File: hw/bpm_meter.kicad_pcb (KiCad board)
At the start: 2 copper layers, 60 x 50 mm, 85 parts, among them J1 Conn_01x06_Pin, J2 Conn_01x03_Pin, J901 USB_C_Receptacle_USB2.0, Q1 AO3400A, SW901 SW_MEC_5E, U1 AOZ1282CI, U10 IS31FL3236A, U11 SLS0391FR1A1GD, U12 SLS0391FR1A1GD, U13 SLS0391FR1A1GD, U2 AMS1117-3.3, U3 H11L1, U901 RP2040, U902 AMS1117-3.3, U903 W25Q128JVS, Y901 Crystal_GND24_Small

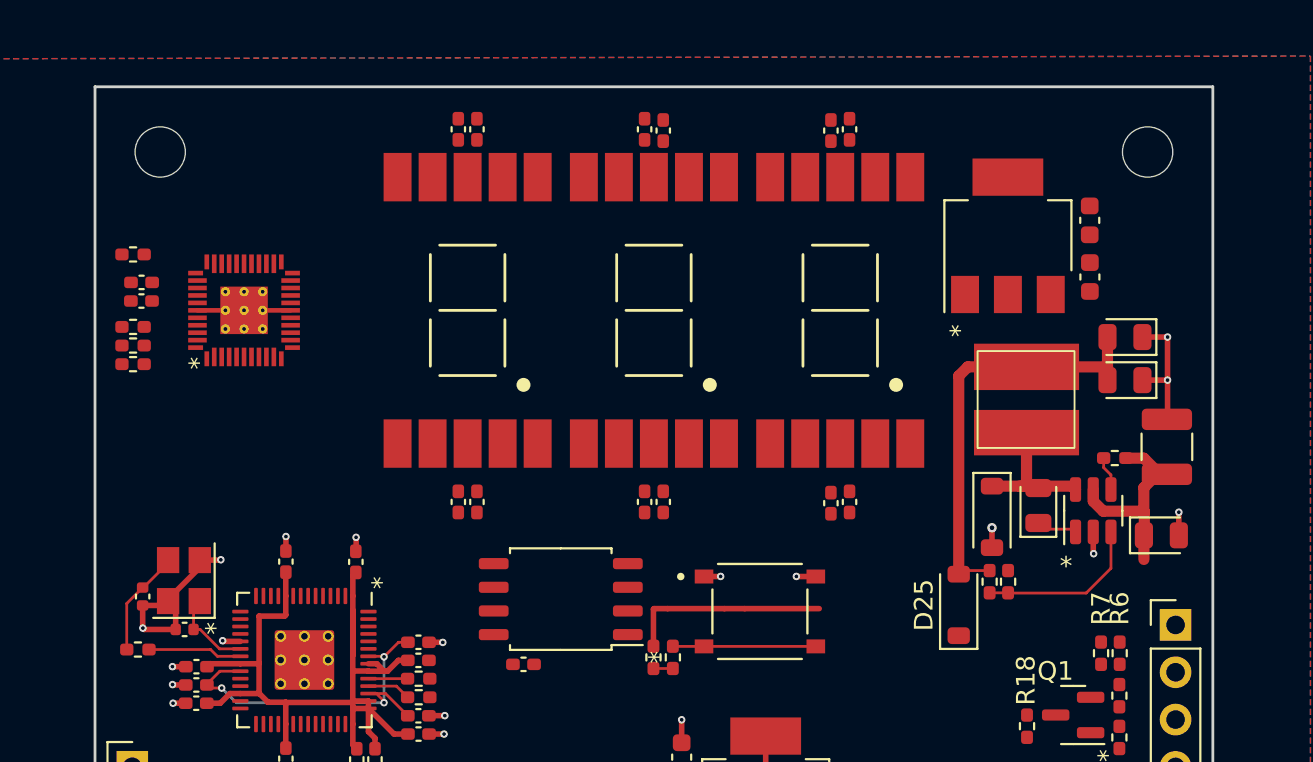
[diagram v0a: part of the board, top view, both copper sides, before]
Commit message: Routed part of the design
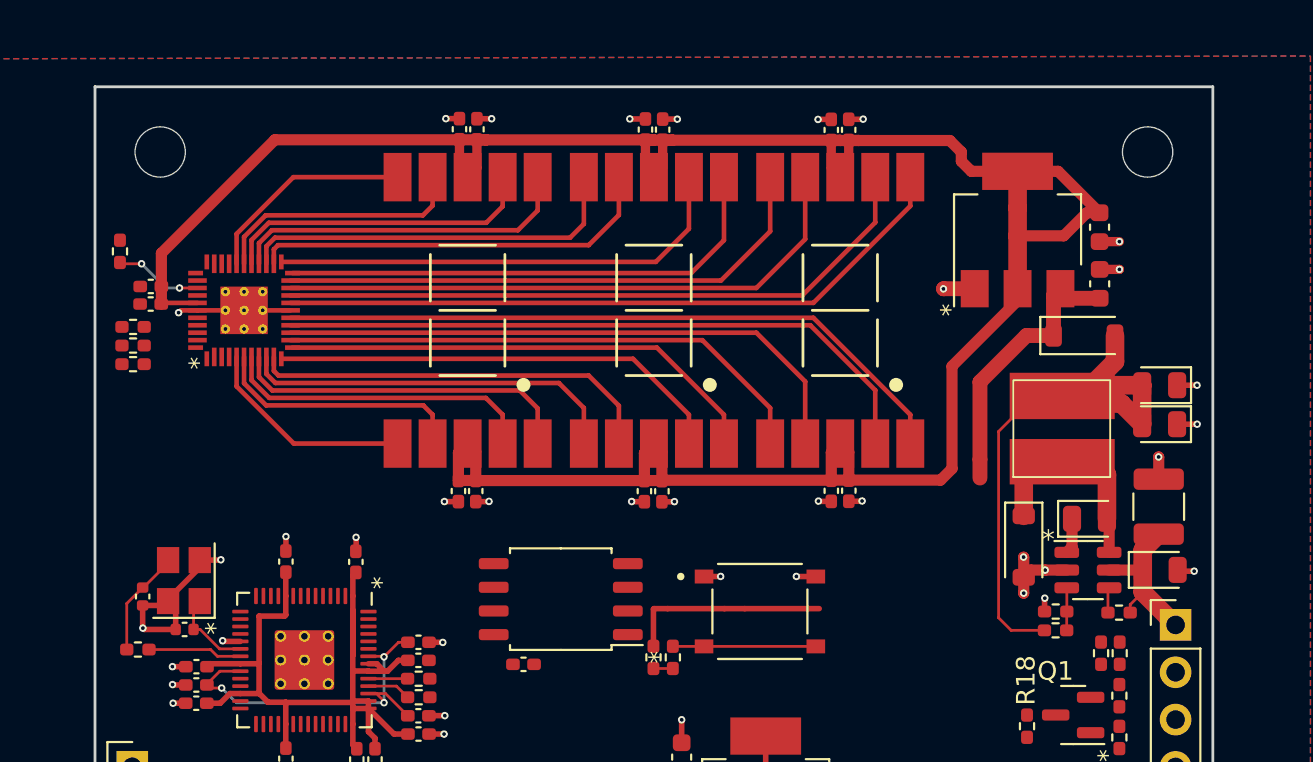
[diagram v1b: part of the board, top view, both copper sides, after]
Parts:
- moved D25 16.0 mm to (153.1, 113.4), turned to 0 degrees
- moved R11 8.30 mm to (155.0, 128.2)
- moved R12 4.40 mm to (151.6, 129.2), turned to 180 degrees
- moved C1 3.24 mm to (157.1, 122.5)
- moved U1 3.20 mm to (153.3, 125.9), turned to 0 degrees
- moved C5 3.19 mm to (157.1, 116.0)
- moved R13 3.02 mm to (151.6, 128.2), turned to 180 degrees
- moved C4 3.01 mm to (157.1, 118.1)
- moved C3 2.84 mm to (153.4, 123.2), turned to 0 degrees
- moved L1 2.47 mm to (152.0, 118.3)
- moved D24 2.33 mm to (149.8, 124.7)
- moved C2 1.86 mm to (157.2, 125.9)
- moved C24 1.26 mm to (103.0, 111.7)
- moved C16 1.17 mm to (140.5, 121.7), turned to -90 degrees
- moved C14 1.17 mm to (129.5, 121.7), turned to -90 degrees
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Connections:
- U10 pad 10: unconnected-(U10-OUT12-Pad10) -> Net-(U10-OUT12)
- U10 pad 11: unconnected-(U10-OUT13-Pad11) -> Net-(U10-OUT13)
- U10 pad 12: unconnected-(U10-OUT14-Pad12) -> Net-(U10-OUT14)
- U10 pad 2: Net-(U10-OUT4) -> unconnected-(U10-OUT4-Pad2)
- U10 pad 22: unconnected-(U10-OUT23-Pad22) -> Net-(U10-OUT23)
- U10 pad 23: unconnected-(U10-OUT24-Pad23) -> Net-(U10-OUT24)
- U10 pad 24: unconnected-(U10-OUT25-Pad24) -> Net-(U10-OUT25)
- U10 pad 3: Net-(U10-OUT5) -> unconnected-(U10-OUT5-Pad3)
- U10 pad 30: Net-(U10-OUT31) -> unconnected-(U10-OUT31-Pad30)
- U10 pad 31: Net-(U10-OUT32) -> unconnected-(U10-OUT32-Pad31)
- U10 pad 32: Net-(U10-OUT33) -> unconnected-(U10-OUT33-Pad32)
- U10 pad 4: Net-(U10-OUT6) -> unconnected-(U10-OUT6-Pad4)
- U11 pad 1: Net-(U10-OUT8) -> Net-(U10-OUT7)
- U11 pad 10: Net-(U10-OUT10) -> Net-(U10-OUT30)
- U11 pad 2: Net-(U10-OUT7) -> Net-(U10-OUT8)
- U11 pad 4: Net-(U10-OUT6) -> Net-(U10-OUT9)
- U11 pad 5: Net-(U10-OUT11) -> Net-(U10-OUT10)
- U11 pad 6: Net-(U10-OUT5) -> Net-(U10-OUT27)
- U11 pad 7: Net-(U10-OUT4) -> Net-(U10-OUT28)
- U11 pad 9: Net-(U10-OUT9) -> Net-(U10-OUT29)
- U12 pad 1: Net-(U10-OUT19) -> Net-(U10-OUT11)
- U12 pad 10: Net-(U10-OUT21) -> Net-(U10-OUT26)
- U12 pad 2: Net-(U10-OUT18) -> Net-(U10-OUT12)
- U12 pad 4: Net-(U10-OUT17) -> Net-(U10-OUT13)
- U12 pad 5: Net-(U10-OUT22) -> Net-(U10-OUT14)
- U12 pad 6: Net-(U10-OUT16) -> Net-(U10-OUT23)
- U12 pad 7: Net-(U10-OUT15) -> Net-(U10-OUT24)
- U12 pad 9: Net-(U10-OUT20) -> Net-(U10-OUT25)
- U13 pad 1: Net-(U10-OUT30) -> Net-(U10-OUT15)
- U13 pad 10: Net-(U10-OUT32) -> Net-(U10-OUT22)
- U13 pad 2: Net-(U10-OUT29) -> Net-(U10-OUT16)
- U13 pad 4: Net-(U10-OUT28) -> Net-(U10-OUT17)
- U13 pad 5: Net-(U10-OUT33) -> Net-(U10-OUT18)
- U13 pad 6: Net-(U10-OUT27) -> Net-(U10-OUT19)
- U13 pad 7: Net-(U10-OUT26) -> Net-(U10-OUT20)
- U13 pad 9: Net-(U10-OUT31) -> Net-(U10-OUT21)
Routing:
- net +3.3VP: track 0.00 -> 137.3 mm
- net Net-(U10-OUT19): track 0.00 -> 37.0 mm
- net Net-(U10-OUT18): track 0.00 -> 37.0 mm
- net Net-(U10-OUT17): track 0.00 -> 35.7 mm
- net Net-(U10-OUT20): track 0.00 -> 35.4 mm
- net Net-(U10-OUT21): track 0.00 -> 32.0 mm
- net Net-(U10-OUT16): track 0.00 -> 32.0 mm
- net Net-(U10-OUT22): track 0.00 -> 29.7 mm
- net Net-(U10-OUT15): track 0.00 -> 29.2 mm
- net Net-(U10-OUT23): track 0.00 -> 27.3 mm
- net Net-(U10-OUT14): track 0.00 -> 26.2 mm
- net Net-(U10-OUT24): track 0.00 -> 25.4 mm
- net Net-(U10-OUT13): track 0.00 -> 24.7 mm
- net Net-(U10-OUT25): track 0.00 -> 22.1 mm
- net Net-(U10-OUT12): track 0.00 -> 22.1 mm
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
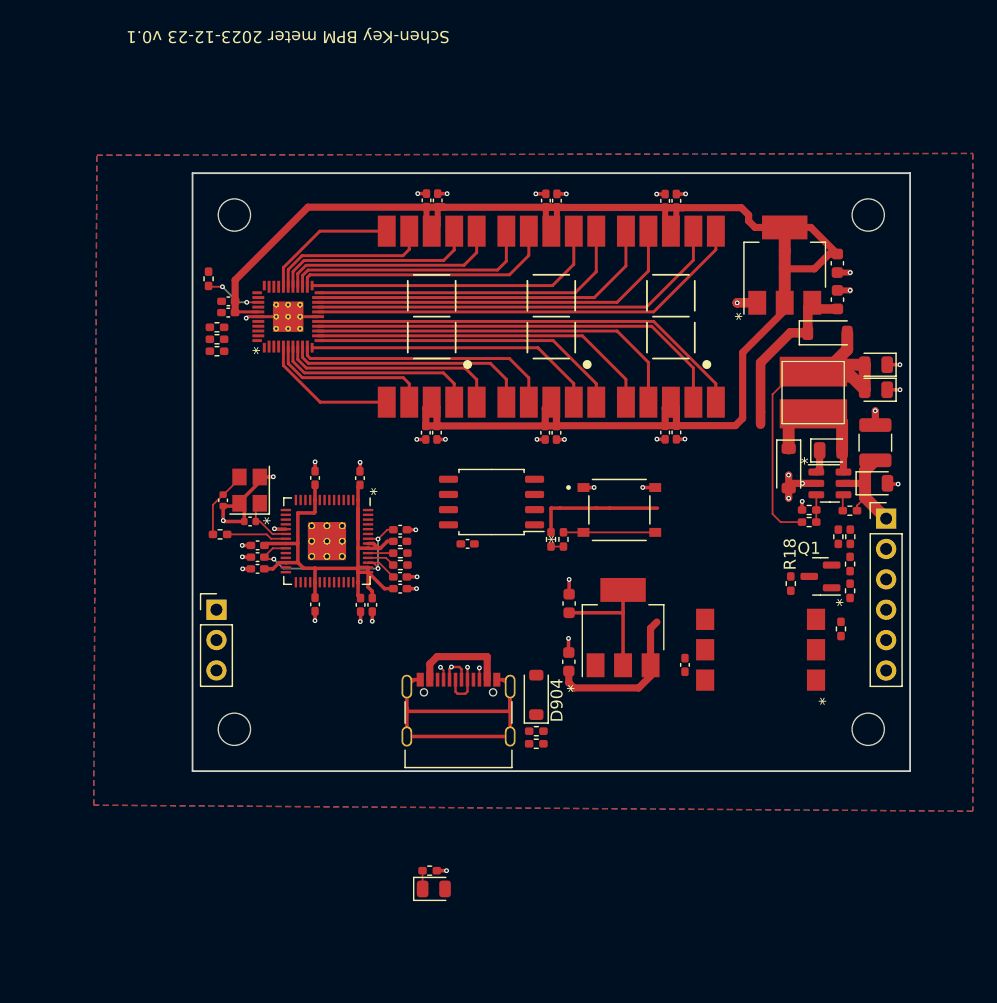
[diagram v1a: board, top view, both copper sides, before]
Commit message: Routed the power supplies and beat inputs
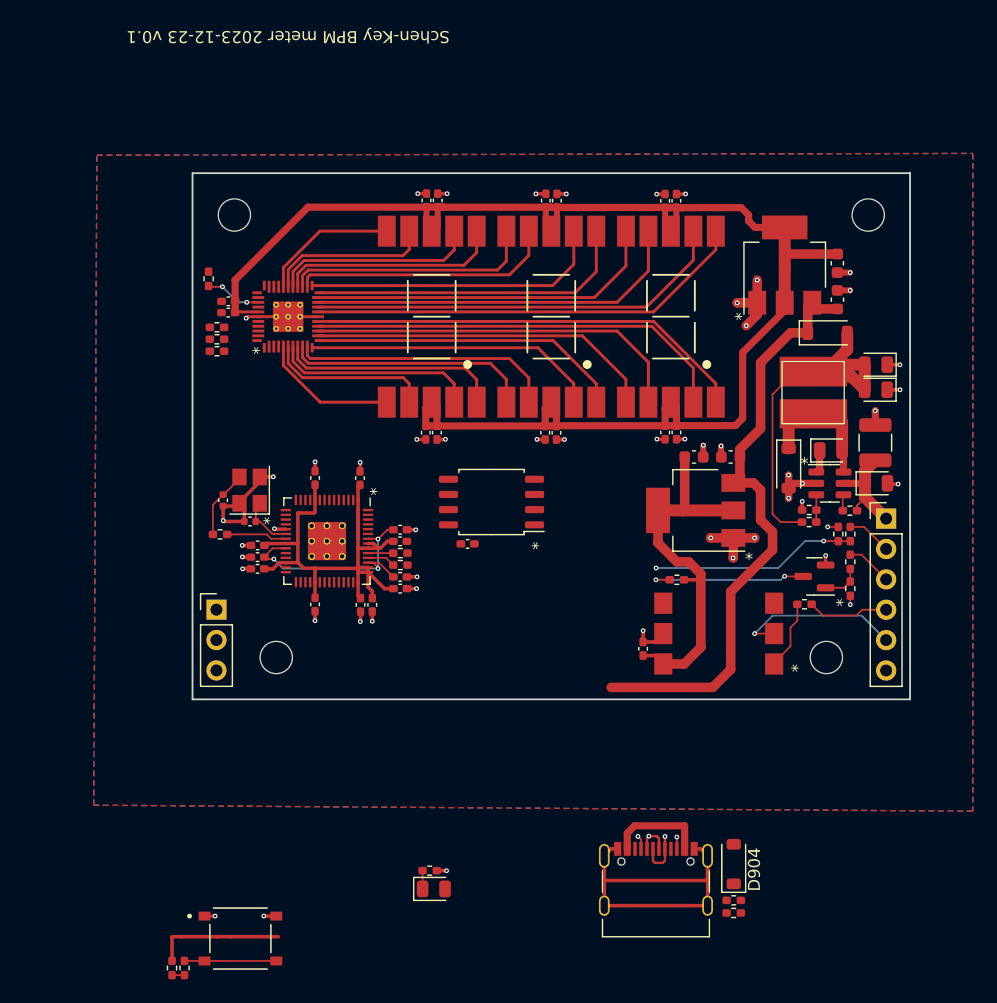
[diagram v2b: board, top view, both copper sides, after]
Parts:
- moved R907 47.8 mm to (98.3, 166.5)
- moved SW901 47.8 mm to (104.0, 164.0)
- moved R906 47.8 mm to (99.3, 166.5)
- moved C901 21.8 mm to (145.0, 123.7), turned to 180 degrees
- moved D904 21.7 mm to (145.3, 157.8)
- moved R901 21.7 mm to (145.3, 161.9)
- moved J901 21.7 mm to (138.8, 159.0)
- moved R902 21.7 mm to (145.3, 160.8)
- moved C902 16.1 mm to (141.9, 123.7), turned to 0 degrees
- moved U902 11.5 mm to (142.1, 128.2), turned to 0 degrees
- moved R18 9.53 mm to (140.5, 134.0), turned to 180 degrees
- moved H1 6.95 mm to (107.0, 140.5)
- moved H4 6.95 mm to (153.0, 140.5)
- moved C10 3.75 mm to (137.7, 139.8)
- moved U3 3.75 mm to (144.0, 138.5)
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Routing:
- net +5V: track 28.3 -> 51.1 mm
- net +3V3: track 66.7 -> 87.3 mm
- net beat_adc: track 0.00 -> 17.2 mm, vias 0 -> 2
- net GND: track 81.6 -> 96.0 mm, vias 43 -> 52
- net Net-(J1-Pin_5): track 0.00 -> 14.1 mm, vias 0 -> 1
- net beat_od: track 0.00 -> 13.6 mm, vias 0 -> 2
- net Net-(J1-Pin_4): track 0.00 -> 6.83 mm
- net Net-(R1-Pad1): track 0.00 -> 5.80 mm
- net +3.3VP: track 137.3 -> 131.6 mm
- net Net-(J1-Pin_3): track 0.00 -> 3.85 mm
- net Net-(J1-Pin_2): track 0.00 -> 3.76 mm
- net Net-(Q1-G): track 0.00 -> 3.33 mm
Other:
- board size 60 x 50 mm -> 60 x 44 mm

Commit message: Routing almost finished, QSPI flash missing
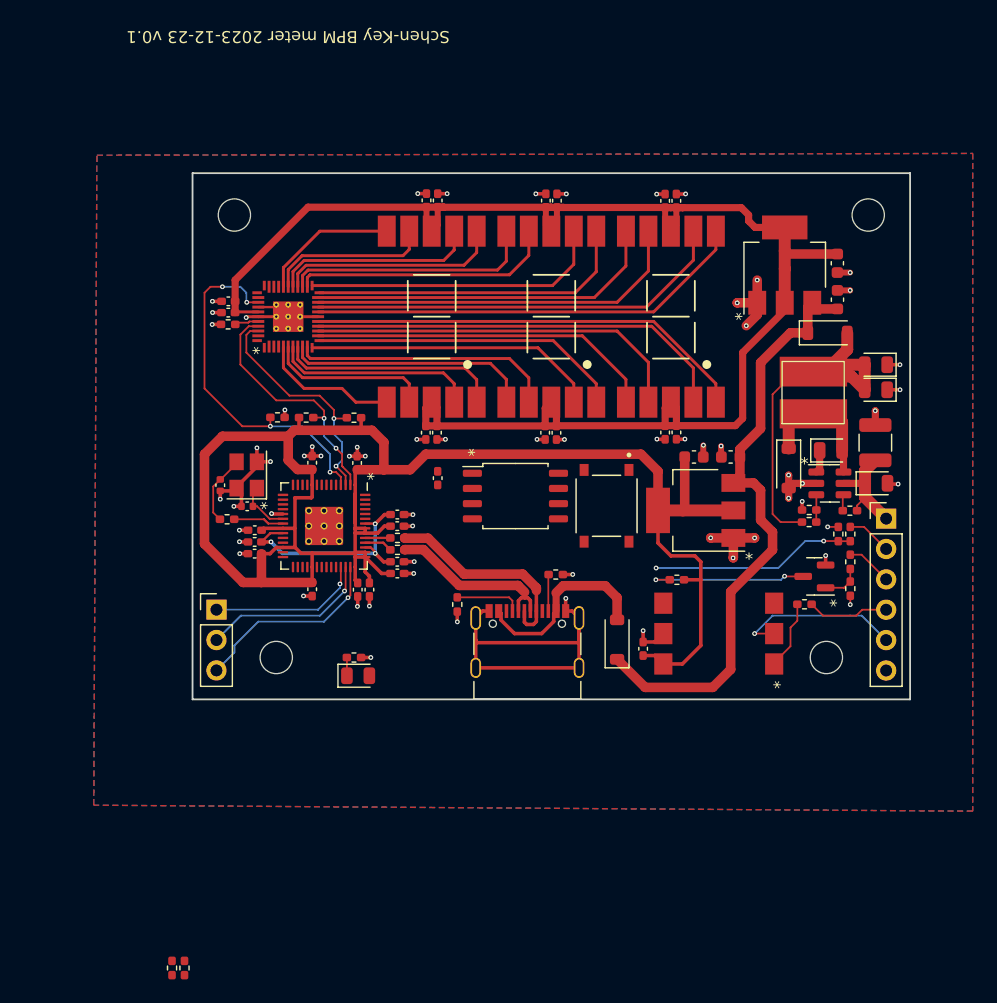
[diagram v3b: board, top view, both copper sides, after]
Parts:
- moved SW901 47.4 mm to (134.6, 127.8), turned to -90 degrees
- moved R901 34.6 mm to (122.1, 136.1), turned to -90 degrees
- moved R902 31.0 mm to (130.4, 133.6)
- moved J901 22.6 mm to (128.0, 139.1)
- moved D904 21.2 mm to (135.5, 139.0)
- moved R905 18.9 mm to (113.5, 140.5)
- moved D901 18.9 mm to (113.8, 142.0)
- moved R5 12.9 mm to (107.1, 120.4), turned to 0 degrees
- moved R3 12.7 mm to (113.5, 120.4), turned to 180 degrees
- moved R4 9.92 mm to (109.5, 120.4)
- moved C912 6.04 mm to (120.5, 125.5), turned to 90 degrees
- moved U903 2.06 mm to (127.0, 127.0), turned to -90 degrees
- moved R908 1.39 mm to (102.9, 128.9)
- moved C908 1.29 mm to (105.2, 129.9)
- moved C910 1.29 mm to (102.3, 126.1)
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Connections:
- U901 pad 36: beat_od -> beat_opto
- U901 pad 37: beat_opto -> beat_od
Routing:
- net +3V3: track 87.3 -> 151.9 mm
- net sdb: track 4.73 -> 30.4 mm, vias 2 -> 4
- net sda: track 0.00 -> 20.9 mm, vias 0 -> 2
- net scl: track 0.00 -> 20.1 mm, vias 0 -> 2
- net Net-(J2-Pin_3): track 0.00 -> 16.5 mm, vias 0 -> 1
- net Net-(J2-Pin_2): track 0.00 -> 14.4 mm, vias 0 -> 1
- net /cpu/USB_D+: track 4.19 -> 17.7 mm, vias 1 -> 0
- net Net-(J2-Pin_1): track 0.00 -> 12.8 mm, vias 0 -> 1
- net /cpu/USB_D-: track 2.93 -> 14.9 mm, vias 1 -> 0
- net GND: track 96.0 -> 104.1 mm, vias 52 -> 64
- net Net-(D904-A): track 8.29 -> 16.2 mm
- net Net-(SW901-A): track 7.66 -> 0.00 mm
- net Net-(J901-CC1): track 1.14 -> 5.60 mm, vias 1 -> 0
- net Net-(U10-R_EXT): track 0.00 -> 2.03 mm
- net Net-(J901-CC2): track 0.99 -> 2.93 mm, vias 1 -> 0
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
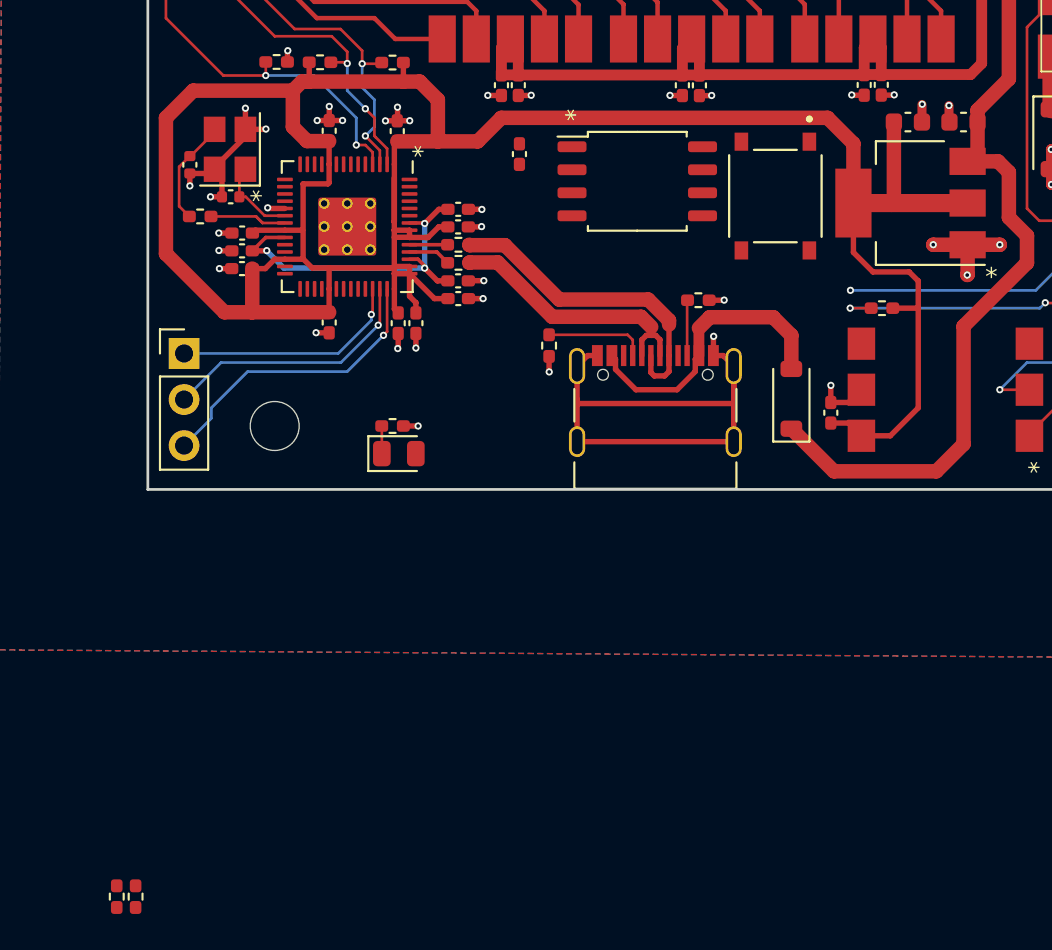
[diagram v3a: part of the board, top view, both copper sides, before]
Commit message: Finished routing all nets
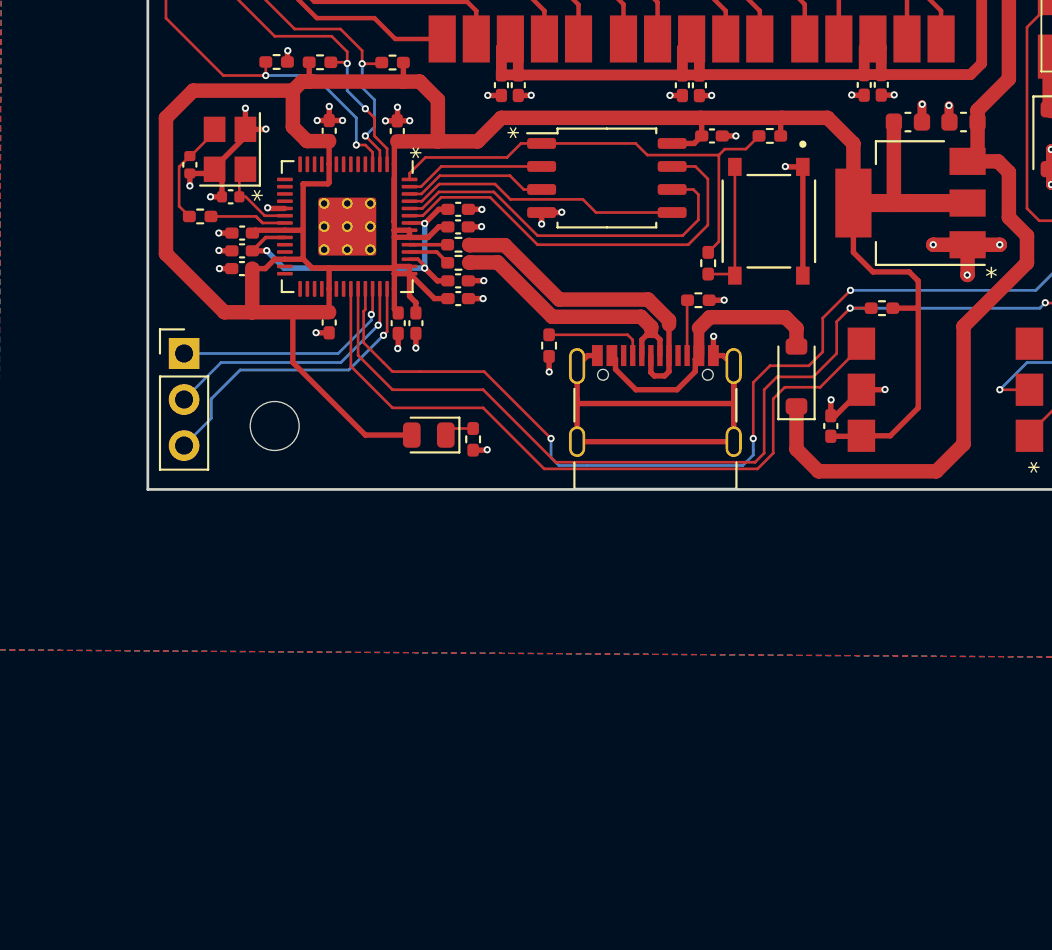
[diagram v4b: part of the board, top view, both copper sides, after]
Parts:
- moved R907 55.3 mm to (134.3, 124.5), turned to 180 degrees
- moved R906 47.1 mm to (130.9, 131.5), turned to 90 degrees
- moved C912 10.7 mm to (131.1, 124.5), turned to 0 degrees
- moved R905 4.51 mm to (117.9, 141.2), turned to 90 degrees
- moved D901 1.94 mm to (115.5, 141.0), turned to 180 degrees
- moved U903 1.69 mm to (125.3, 126.8)
- moved SW901 1.44 mm to (134.3, 129.2)
- moved D904 1.27 mm to (135.8, 137.8)
- moved C10 0.73 mm to (137.7, 140.5)
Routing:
- net beat_adc: track 17.2 -> 57.9 mm, vias 2 -> 4
- net beat_od: track 13.6 -> 53.5 mm
- net beat_opto: track 0.00 -> 39.5 mm
- net /cpu/QSPI_SS: track 0.00 -> 26.6 mm
- net /cpu/QSPI_SD3: track 0.00 -> 23.2 mm
- net /cpu/QSPI_SCLK: track 0.00 -> 20.6 mm
- net /cpu/QSPI_SD0: track 0.00 -> 15.5 mm
- net +3V3: track 151.9 -> 166.6 mm
- net GND: track 104.1 -> 115.1 mm, vias 64 -> 69
- net /cpu/QSPI_SD2: track 0.00 -> 8.02 mm
- net /cpu/QSPI_SD1: track 0.00 -> 7.75 mm
- net Net-(SW901-A): track 0.00 -> 7.51 mm
- net +5V: track 51.6 -> 53.2 mm
- net Net-(D904-A): track 16.2 -> 15.5 mm

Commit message: Minor optimizations
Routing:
- net GND: track 115.1 -> 120.3 mm, vias 69 -> 133
- net +3V3: track 166.6 -> 171.6 mm
- net Net-(D25-A): track 33.7 -> 36.3 mm
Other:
- board text added: "${COMPANY} ${TITLE} ${REVISION}"
- board text removed: "${TITLE} ${ISSUE_DATE} v${REVISION}"
